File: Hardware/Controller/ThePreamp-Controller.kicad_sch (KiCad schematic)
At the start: 12 parts, among them J1 Digital Out, J14 12V, J15 8V, J2 SPI DISPLAY 2, J9 SPI DISPLAY 1, SW1 RotaryEncoder_Switch, SW2 RotaryEncoder_Switch, U1 TSOP34838, U5 24C02C_SN, U6 ESP32-DEVKIT-V1

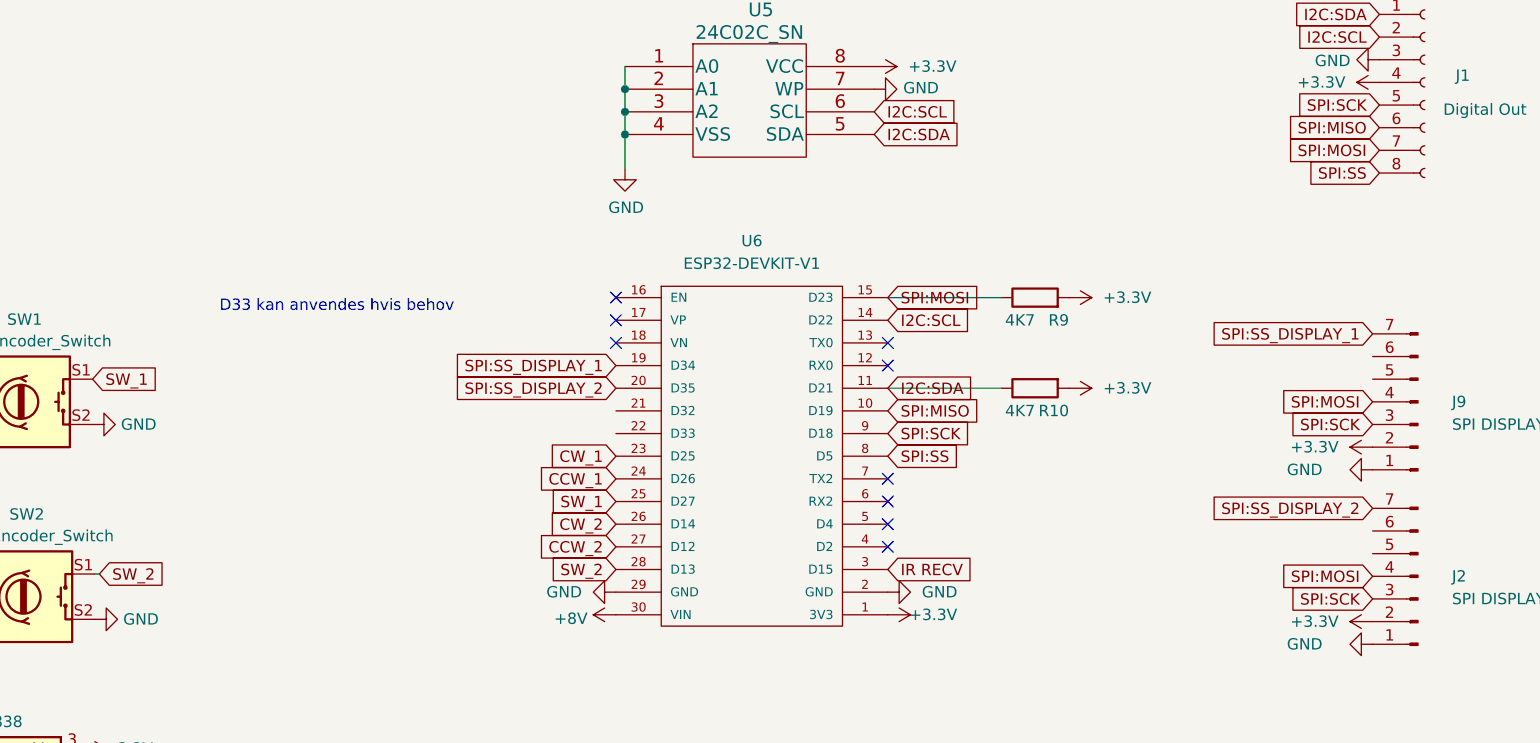
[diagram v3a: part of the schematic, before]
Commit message: Pins updated
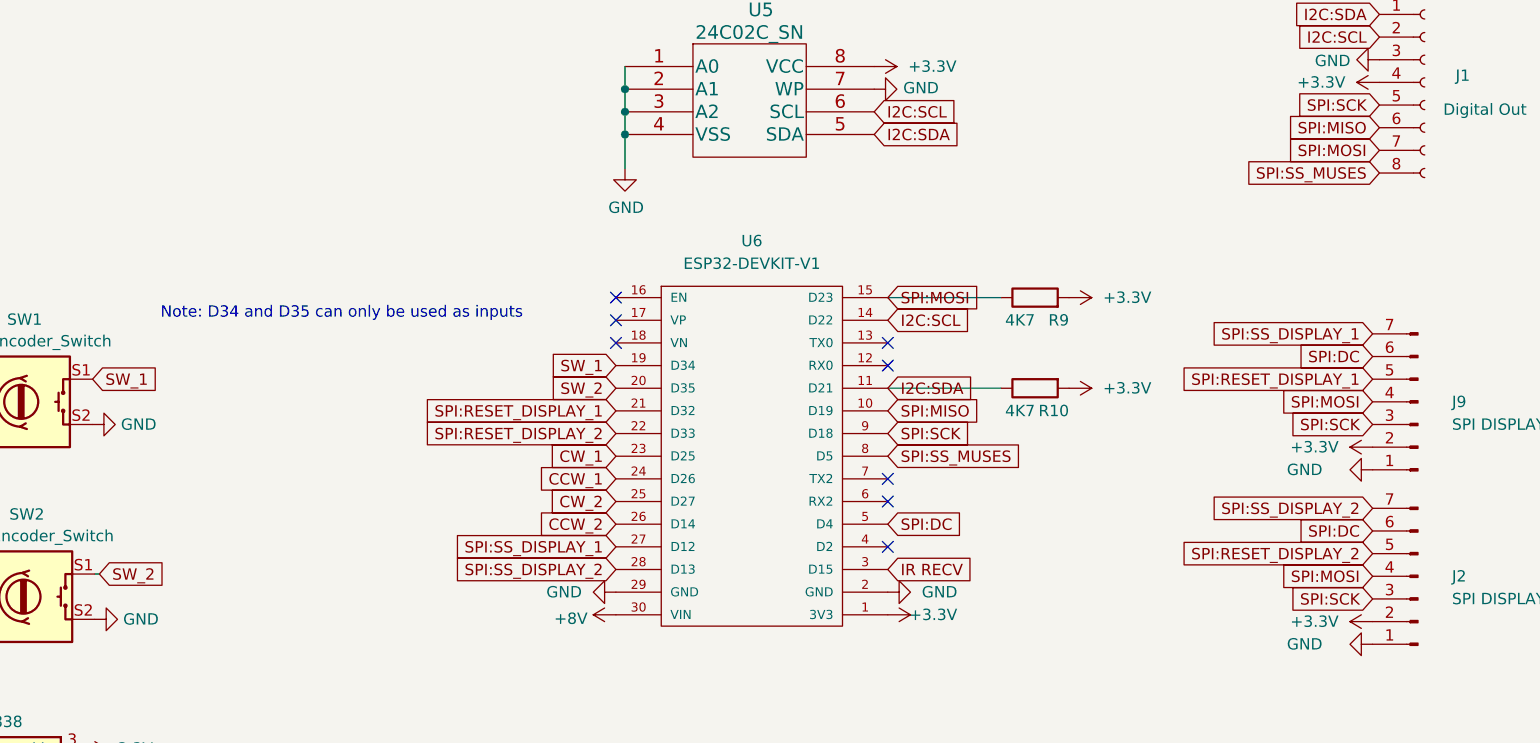
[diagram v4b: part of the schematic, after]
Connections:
- net CCW_2: now also U6.26 (D14); no longer U6.27 (D12)
- net CW_2: now also U6.25 (D27); no longer U6.26 (D14)
- net SPI:SS_DISPLAY_1: now also U6.27 (D12); no longer U6.19 (D34)
- net SPI:SS_DISPLAY_2: now also U6.28 (D13); no longer U6.20 (D35)
- net SW_1: now also U6.19 (D34); no longer U6.25 (D27)
- net SW_2: now also U6.20 (D35); no longer U6.28 (D13)
- net SPI:RESET_DISPLAY_1: now reaches J9.5 (Pin_5)
- net SPI:RESET_DISPLAY_1: now also U6.21 (D32)
- net SPI:DC: now reaches J9.6 (Pin_6)
- net SPI:DC: now also J2.6 (Pin_6), U6.5 (D4)
- net SPI:RESET_DISPLAY_2: now reaches U6.22 (D33)
- net SPI:RESET_DISPLAY_2: now also J2.5 (Pin_5)
- net SPI:SS renamed SPI:SS_MUSES
- no-connect marks 9 -> 8
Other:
- note added: "Note: D34 and D35 can only be used as inputs"
- note removed: "D33 kan anvendes hvis behov"
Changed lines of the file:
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@@
   (no_connect (at 187.96 78.74))
   (no_connect (at 187.96 81.28))
-  (no_connect (at 187.96 99.06))
   (no_connect (at 187.96 101.6))
   (no_connect (at 157.48 78.74))
@@
     (stroke (width 0) (type default))
   )
-  (text "D33 kan anvendes hvis behov" (at 113.03 75.438 0)
+  (text "Note: D34 and D35 can only be used as inputs" (at 106.426 76.2 0)
     (effects (font (size 1.27 1.27)) (justify left bottom))
   )
-  (global_label "SW_1" (shape input) (at 157.48 96.52 180) (fields_autoplaced)
-    (effects (font (size 1.27 1.27)) (justify right))
-    (property "Intersheetrefs" "${INTERSHEET_REFS}" (at 150.3177 96.4406 0)
+  (global_label "SW_1" (shape input) (at 157.48 81.28 180) (fields_autoplaced)
+    (effects (font (size 1.27 1.27)) (justify right))
+    (property "Intersheetrefs" "${INTERSHEET_REFS}" (at 150.3177 81.2006 0)
+      (effects (font (size 1.27 1.27)) (justify right) hide)
+    )
+  )
+  (global_label "SPI:RESET_DISPLAY_2" (shape input) (at 157.48 88.9 180) (fields_autoplaced)
+    (effects (font (size 1.27 1.27)) (justify right))
+    (property "Intersheetrefs" "${INTERSHEET_REFS}" (at 135.0105 88.9 0)
       (effects (font (size 1.27 1.27)) (justify right) hide)
     )
@@
     )
   )
+  (global_label "SPI:DC" (shape input) (at 242.316 80.264 180) (fields_autoplaced)
+    (effects (font (size 1.27 1.27)) (justify right))
+    (property "Intersheetrefs" "${INTERSHEET_REFS}" (at 233.7559 80.264 0)
+      (effects (font (size 1.27 1.27)) (justify right) hide)
+    )
+  )
   (global_label "SPI:MOSI" (shape input) (at 242.316 104.902 180) (fields_autoplaced)
     (effects (font (size 1.27 1.27)) (justify right))
@@
     )
   )
-  (global_label "SPI:SS_DISPLAY_2" (shape input) (at 157.48 83.82 180) (fields_autoplaced)
-    (effects (font (size 1.27 1.27)) (justify right))
-    (property "Intersheetrefs" "${INTERSHEET_REFS}" (at 138.3366 83.82 0)
+  (global_label "SPI:SS_DISPLAY_2" (shape input) (at 157.48 104.14 180) (fields_autoplaced)
+    (effects (font (size 1.27 1.27)) (justify right))
+    (property "Intersheetrefs" "${INTERSHEET_REFS}" (at 138.3366 104.14 0)
       (effects (font (size 1.27 1.27)) (justify right) hide)
     )
@@
     )
   )
+  (global_label "SPI:DC" (shape input) (at 187.96 99.06 0) (fields_autoplaced)
+    (effects (font (size 1.27 1.27)) (justify left))
+    (property "Intersheetrefs" "${INTERSHEET_REFS}" (at 196.5201 99.06 0)
+      (effects (font (size 1.27 1.27)) (justify left) hide)
+    )
+  )
   (global_label "CCW_1" (shape input) (at 77.724 87.376 180) (fields_autoplaced)
     (effects (font (size 1.27 1.27)) (justify right))
@@
     )
   )
-  (global_label "CW_2" (shape input) (at 157.48 99.06 180) (fields_autoplaced)
-    (effects (font (size 1.27 1.27)) (justify right))
-    (property "Intersheetrefs" "${INTERSHEET_REFS}" (at 150.2572 99.1394 0)
+  (global_label "CW_2" (shape input) (at 157.48 96.52 180) (fields_autoplaced)
+    (effects (font (size 1.27 1.27)) (justify right))
+    (property "Intersheetrefs" "${INTERSHEET_REFS}" (at 150.2572 96.5994 0)
+      (effects (font (size 1.27 1.27)) (justify right) hide)
+    )
+  )
+  (global_label "SPI:DC" (shape input) (at 242.316 99.822 180) (fields_autoplaced)
+    (effects (font (size 1.27 1.27)) (justify right))
+    (property "Intersheetrefs" "${INTERSHEET_REFS}" (at 233.7559 99.822 0)
       (effects (font (size 1.27 1.27)) (justify right) hide)
     )
@@
     )
   )
-  (global_label "SW_2" (shape input) (at 157.48 104.14 180) (fields_autoplaced)
-    (effects (font (size 1.27 1.27)) (justify right))
-    (property "Intersheetrefs" "${INTERSHEET_REFS}" (at 150.3177 104.2194 0)
-      (effects (font (size 1.27 1.27)) (justify right) hide)
-    )
-  )
-  (global_label "SPI:SS" (shape input) (at 187.96 91.44 0) (fields_autoplaced)
-    (effects (font (size 1.27 1.27)) (justify left))
-    (property "Intersheetrefs" "${INTERSHEET_REFS}" (at -45.72 36.83 0)
-      (effects (font (size 1.27 1.27)) hide)
+  (global_label "SW_2" (shape input) (at 157.48 83.82 180) (fields_autoplaced)
+    (effects (font (size 1.27 1.27)) (justify right))
+    (property "Intersheetrefs" "${INTERSHEET_REFS}" (at 150.3177 83.8994 0)
+      (effects (font (size 1.27 1.27)) (justify right) hide)
+    )
+  )
+  (global_label "SPI:SS_MUSES" (shape input) (at 187.96 91.44 0) (fields_autoplaced)
+    (effects (font (size 1.27 1.27)) (justify left))
+    (property "Intersheetrefs" "${INTERSHEET_REFS}" (at 203.7166 91.44 0)
+      (effects (font (size 1.27 1.27)) (justify left) hide)
     )
   )
@@
     )
   )
-  (global_label "SPI:SS" (shape input) (at 243.078 59.69 180) (fields_autoplaced)
-    (effects (font (size 1.27 1.27)) (justify right))
-    (property "Intersheetrefs" "${INTERSHEET_REFS}" (at 476.758 114.3 0)
-      (effects (font (size 1.27 1.27)) hide)
+  (global_label "SPI:SS_MUSES" (shape input) (at 243.078 59.69 180) (fields_autoplaced)
+    (effects (font (size 1.27 1.27)) (justify right))
+    (property "Intersheetrefs" "${INTERSHEET_REFS}" (at 227.3214 59.69 0)
+      (effects (font (size 1.27 1.27)) (justify right) hide)
     )
   )
@@
     )
   )
+  (global_label "SPI:RESET_DISPLAY_2" (shape input) (at 242.316 102.362 180) (fields_autoplaced)
+    (effects (font (size 1.27 1.27)) (justify right))
+    (property "Intersheetrefs" "${INTERSHEET_REFS}" (at 219.8465 102.362 0)
+      (effects (font (size 1.27 1.27)) (justify right) hide)
+    )
+  )
   (global_label "SPI:SCK" (shape input) (at 242.316 87.884 180) (fields_autoplaced)
     (effects (font (size 1.27 1.27)) (justify right))
@@
     (property "Intersheetrefs" "${INTERSHEET_REFS}" (at 195.9637 52.832 0)
       (effects (font (size 1.27 1.27)) (justify left) hide)
+    )
+  )
+  (global_label "SPI:RESET_DISPLAY_1" (shape input) (at 157.48 86.36 180) (fields_autoplaced)
+    (effects (font (size 1.27 1.27)) (justify right))
+    (property "Intersheetrefs" "${INTERSHEET_REFS}" (at 135.0105 86.36 0)
+      (effects (font (size 1.27 1.27)) (justify right) hide)
     )
   )
@@
     )
   )
+  (global_label "SPI:RESET_DISPLAY_1" (shape input) (at 242.316 82.804 180) (fields_autoplaced)
+    (effects (font (size 1.27 1.27)) (justify right))
+    (property "Intersheetrefs" "${INTERSHEET_REFS}" (at 219.8465 82.804 0)
+      (effects (font (size 1.27 1.27)) (justify right) hide)
+    )
+  )
   (global_label "SPI:MOSI" (shape input) (at 187.96 73.66 0) (fields_autoplaced)
     (effects (font (size 1.27 1.27)) (justify left))
@@
     )
   )
-  (global_label "SPI:SS_DISPLAY_1" (shape input) (at 157.48 81.28 180) (fields_autoplaced)
-    (effects (font (size 1.27 1.27)) (justify right))
-    (property "Intersheetrefs" "${INTERSHEET_REFS}" (at 138.3366 81.28 0)
-      (effects (font (size 1.27 1.27)) (justify right) hide)
-    )
-  )
-  (global_label "CCW_2" (shape input) (at 157.48 101.6 180) (fields_autoplaced)
-    (effects (font (size 1.27 1.27)) (justify right))
-    (property "Intersheetrefs" "${INTERSHEET_REFS}" (at 148.9872 101.6794 0)
-      (effects (font (size 1.27 1.27)) (justify right) hide)
-    )
+  (global_label "SPI:SS_DISPLAY_1" (shape input) (at 157.48 101.6 180) (fields_autoplaced)
+    (effects (font (size 1.27 1.27)) (justify right))
+    (property "Intersheetrefs" "${INTERSHEET_REFS}" (at 138.3366 101.6 0)
+      (effects (font (size 1.27 1.27)) (justify right) hide)
+    )
+  )
+  (global_label "CCW_2" (shape input) (at 157.48 99.06 180) (fields_autoplaced)
+    (effects (font (size 1.27 1.27)) (justify right))
+    (property "Intersheetrefs" "${INTERSHEET_REFS}" (at 148.9872 99.1394 0)
+      (effects (font (size 1.27 1.27)) (justify right) hide)
+    )

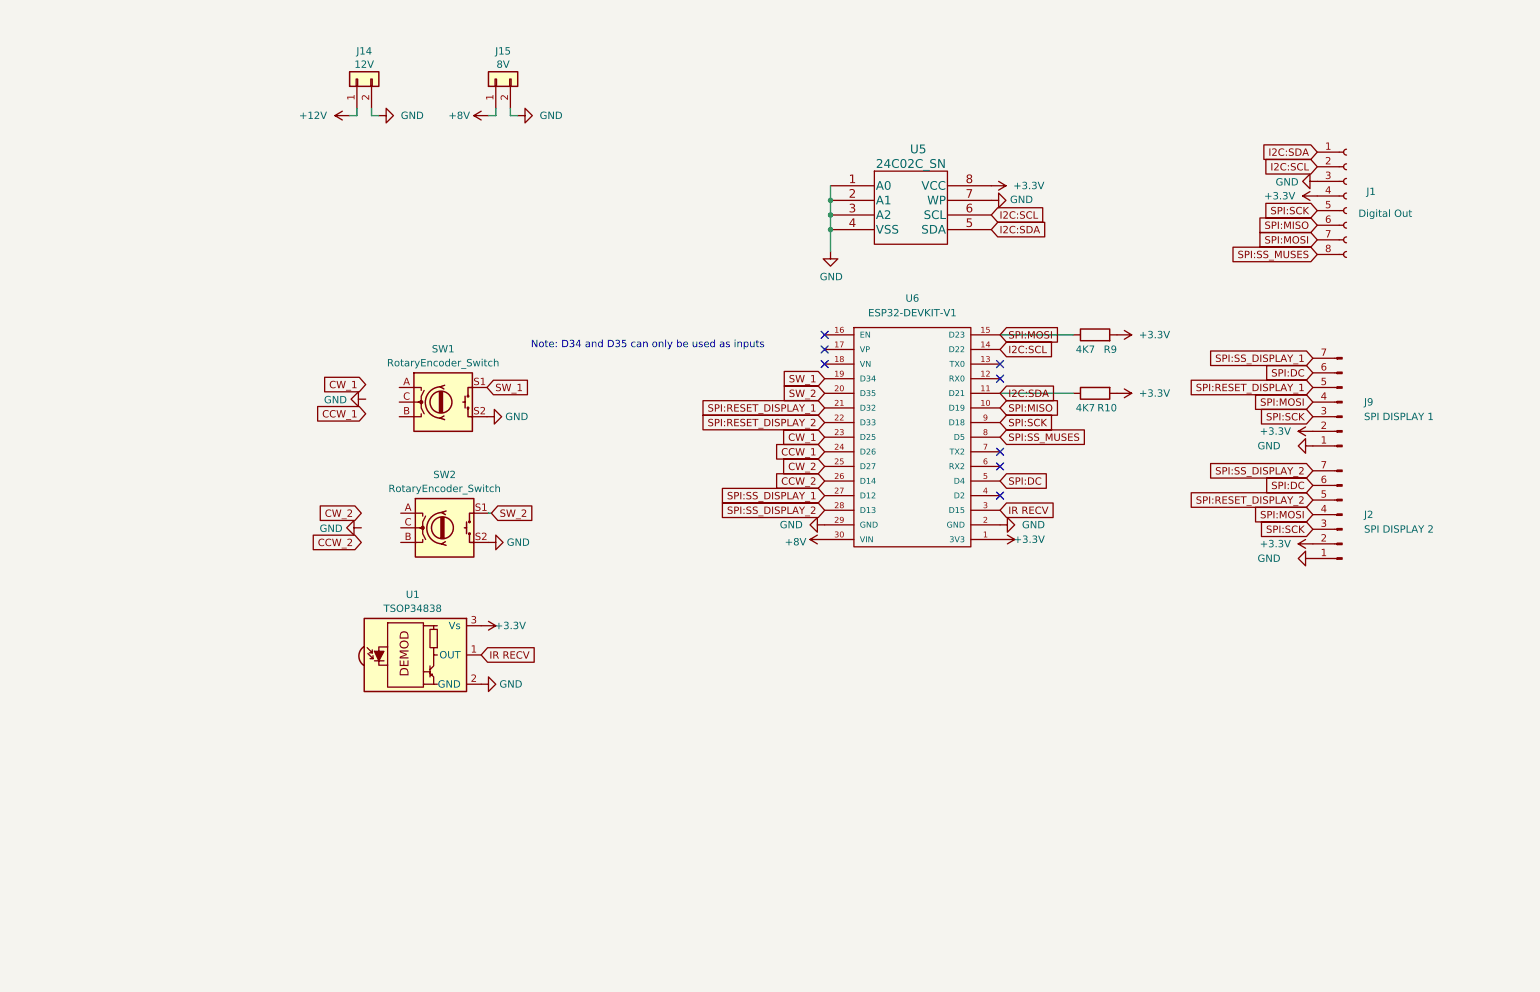
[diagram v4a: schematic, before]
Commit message: Add power relay control output
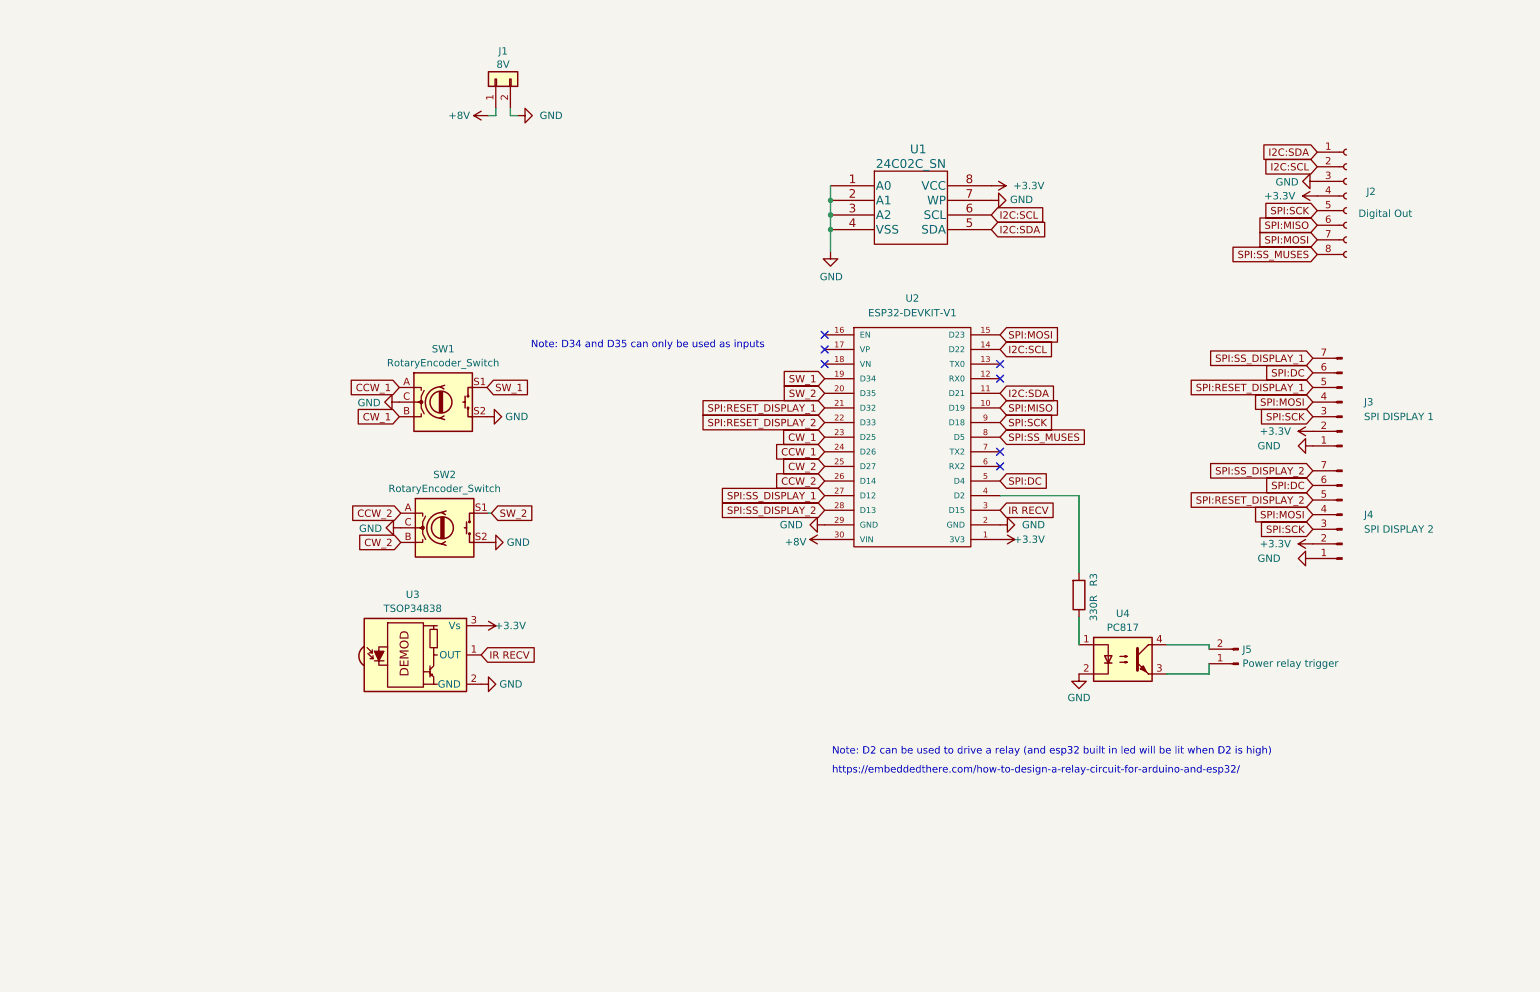
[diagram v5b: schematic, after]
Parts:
- removed J14: 12V, TerminalBlock:TerminalBlock_bornier-2_P5.08mm, symbol Connector_Generic:Conn_01x02
- removed R10, R9: 4K7, Resistor_SMD:R_0805_2012Metric_Pad1.15x1.40mm_HandSolder, symbol Device:R
- added J5: Power relay trigger, Connector_JST:JST_XH_B2B-XH-AM_1x02_P2.50mm_Vertical, symbol Connector:Conn_01x02_Pin
- added R3: 330R, Resistor_SMD:R_0805_2012Metric_Pad1.20x1.40mm_HandSolder, symbol Device:R
- added U4: PC817, Package_DIP:DIP-4_W7.62mm, symbol Isolator:PC817
- renumbered J15 to J1, J1 to J2, J9 to J3, J2 to J4, U5 to U1, U6 to U2, U1 to U3
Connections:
- net CCW_1: now also SW1.A
- net CCW_2: now also SW2.A
- net CW_1: now also SW1.B
- net CW_2: now also SW2.B
- net GND: now also SW1.C, SW2.C, U4.2
- net at U2.4 (D2): now also R3.2
- new net: R3.1, U4.1
- new net: J5.1 (Pin_1), U4.3
- new net: J5.2 (Pin_2), U4.4
- no-connect marks 8 -> 7
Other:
- note added: "Note: D2 can be used to drive a relay (and esp32 built in led will be lit when D2 is high)"
- note added: "https://embeddedthere.com/how-to-design-a-relay-circuit-for-arduino-and-esp32/"
